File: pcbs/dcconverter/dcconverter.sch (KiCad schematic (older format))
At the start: 49 parts, among them IC1 NCP7805TG, J1 190-9991, J2 Conn_01x01, J3 Conn_01x01, J4 146-8335, J5 Conn_01x01, J6 Conn_01x01, J7 766-6604, J8 766-6604, Q1 NGTB40N120FL2WG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

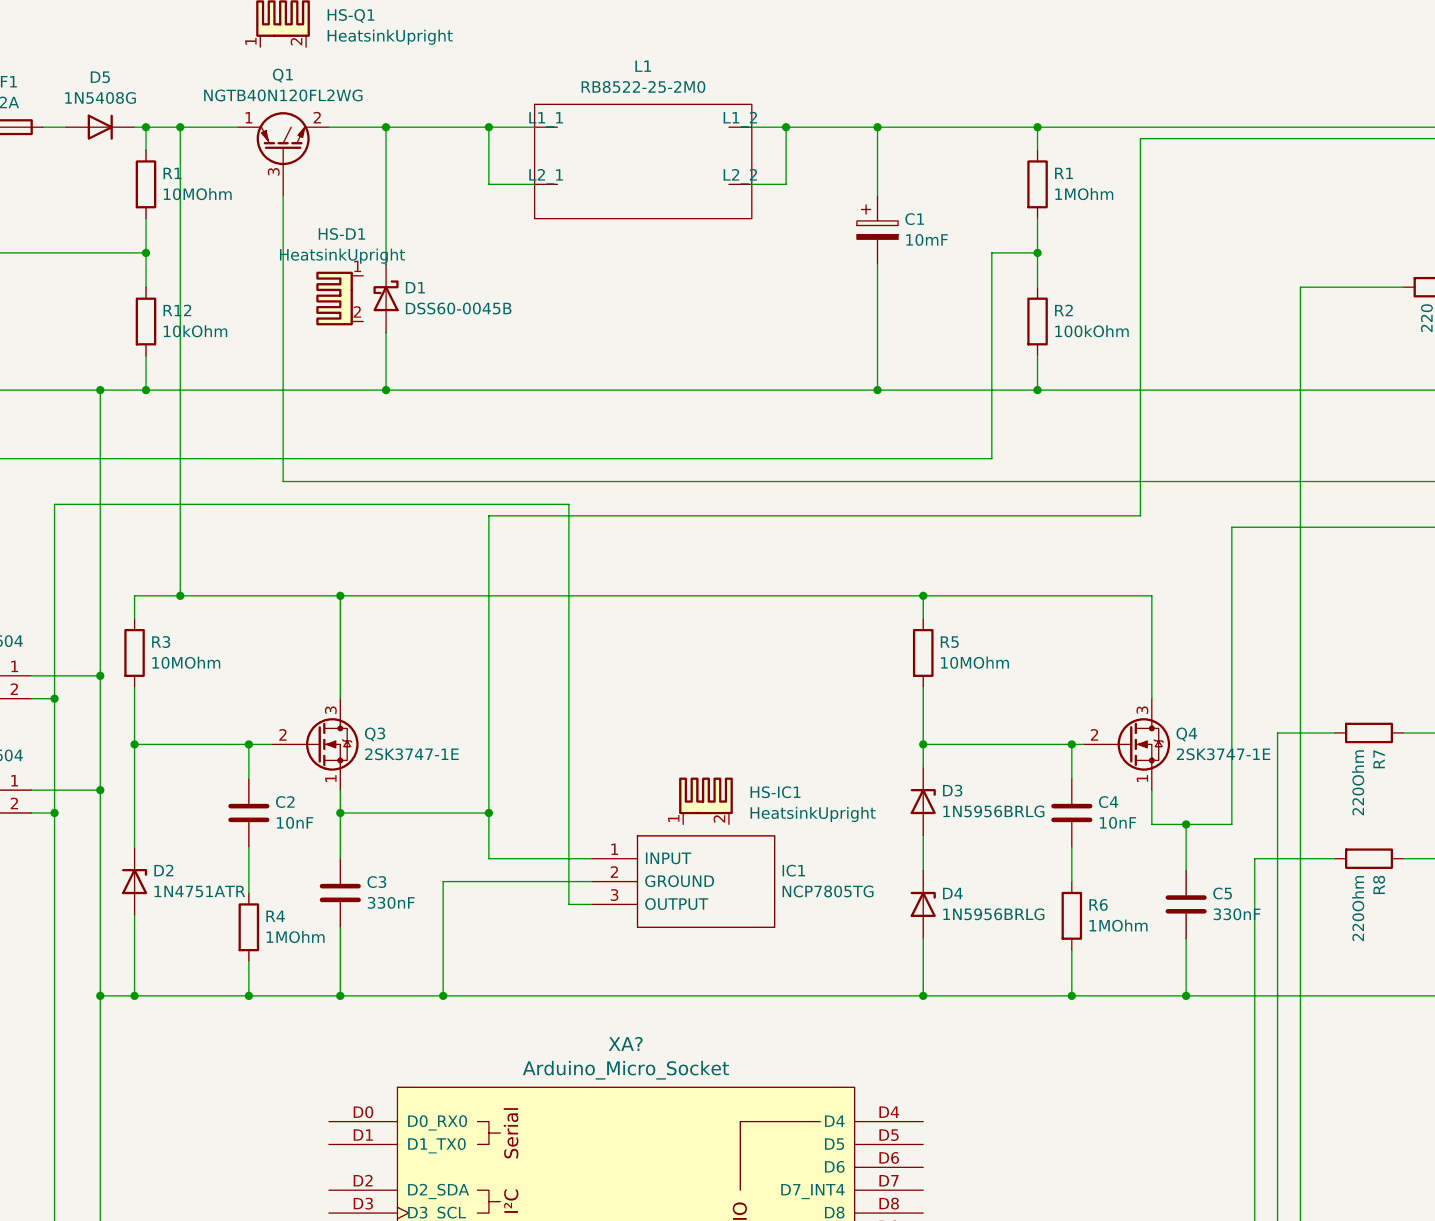
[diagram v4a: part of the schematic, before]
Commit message: Add missing footprints
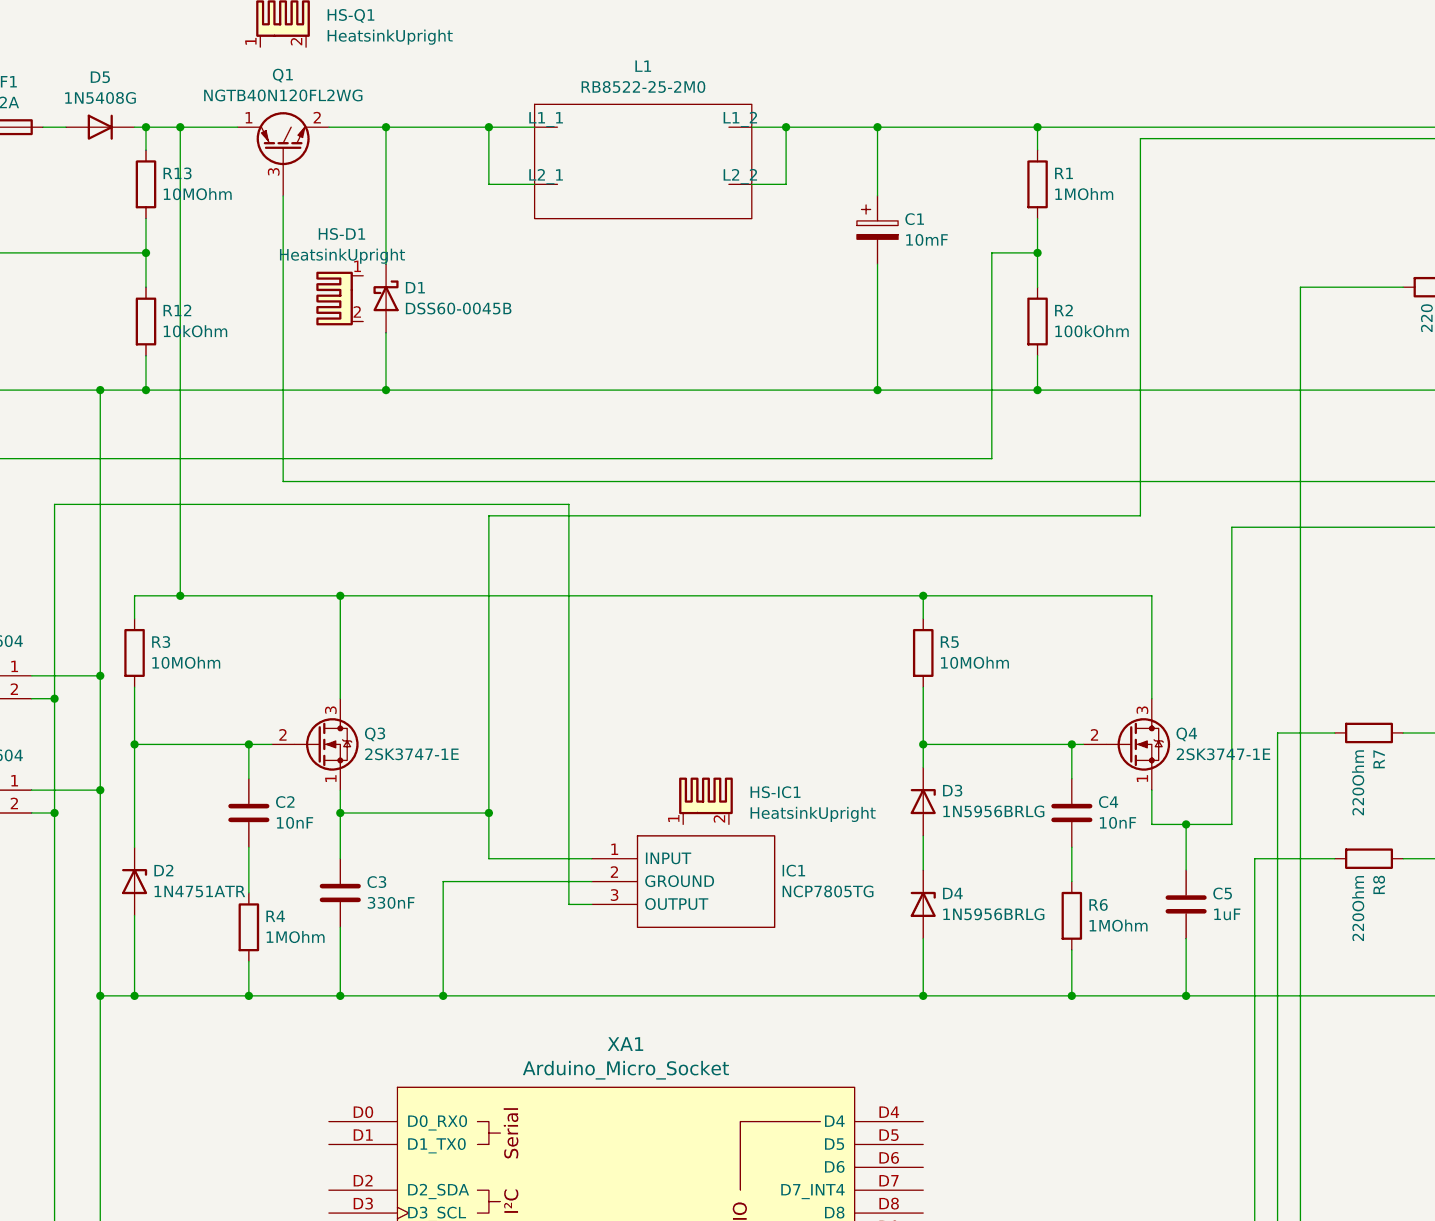
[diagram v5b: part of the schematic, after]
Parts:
- C2, C4: footprint (none) -> Capacitor_THT:C_Disc_D14.5mm_W5.0mm_P7.50mm
- C5: value 330nF -> 1uF; footprint (none) -> Capacitor_THT:CP_Radial_D5.0mm_P2.00mm
- gave numbers to parts that had none: 1
- renumbered R1 to R13
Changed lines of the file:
@@
 F 0 "C2" H 2415 4246 50  0000 L CNN
 F 1 "10nF" H 2415 4155 50  0000 L CNN
-F 2 "" H 2338 4050 50  0001 C CNN
+F 2 "Capacitor_THT:C_Disc_D14.5mm_W5.0mm_P7.50mm" H 2338 4050 50  0001 C CNN
 F 3 "~" H 2300 4200 50  0001 C CNN
 	1    2300 4200
@@
 F 0 "C4" H 6015 4246 50  0000 L CNN
 F 1 "10nF" H 6015 4155 50  0000 L CNN
-F 2 "" H 5938 4050 50  0001 C CNN
+F 2 "Capacitor_THT:C_Disc_D14.5mm_W5.0mm_P7.50mm" H 5938 4050 50  0001 C CNN
 F 3 "~" H 5900 4200 50  0001 C CNN
 	1    5900 4200
@@
 P 6400 4600
 F 0 "C5" H 6515 4646 50  0000 L CNN
-F 1 "330nF" H 6515 4555 50  0000 L CNN
-F 2 "" H 6438 4450 50  0001 C CNN
+F 1 "1uF" H 6515 4555 50  0000 L CNN
+F 2 "Capacitor_THT:CP_Radial_D5.0mm_P2.00mm" H 6438 4450 50  0001 C CNN
 F 3 "~" H 6400 4600 50  0001 C CNN
 	1    6400 4600
@@
 	1650 2350 1850 2350
 $Comp
-L Device:R R1
+L Device:R R13
 U 1 1 5FBBC80C
 P 1850 1450
-F 0 "R1" H 1920 1496 50  0000 L CNN
+F 0 "R13" H 1920 1496 50  0000 L CNN
 F 1 "10MOhm" H 1920 1405 50  0000 L CNN
 F 2 "Resistor_THT:R_Axial_DIN0207_L6.3mm_D2.5mm_P10.16mm_Horizontal" V 1780 1450 50  0001 C CNN
@@
 	1850 2350 2900 2350
 $Comp
-L Custom:Arduino_Micro_Socket XA?
+L Custom:Arduino_Micro_Socket XA1
 U 1 1 5FBF5E9B
 P 3950 6450
-F 0 "XA?" H 3950 7687 60  0000 C CNN
+F 0 "XA1" H 3950 7687 60  0000 C CNN
 F 1 "Arduino_Micro_Socket" H 3950 7581 60  0000 C CNN
 F 2 "Custom:Arduino_Micro_Socket" H 5750 10200 60  0001 C CNN

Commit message: Empty PCB
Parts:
- C3: value 330nF -> 1uF; footprint (none) -> Capacitor_THT:CP_Radial_D5.0mm_P2.00mm
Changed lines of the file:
@@
 P 2700 4550
 F 0 "C3" H 2815 4596 50  0000 L CNN
-F 1 "330nF" H 2815 4505 50  0000 L CNN
-F 2 "" H 2738 4400 50  0001 C CNN
+F 1 "1uF" H 2815 4505 50  0000 L CNN
+F 2 "Capacitor_THT:CP_Radial_D5.0mm_P2.00mm" H 2738 4400 50  0001 C CNN
 F 3 "~" H 2700 4550 50  0001 C CNN
 	1    2700 4550

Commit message: Fix Heatsinks
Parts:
- C3, C5: footprint Capacitor_THT:CP_Radial_D5.0mm_P2.00mm -> Capacitor_THT:CP_Radial_D8.0mm_P2.50mm
- HS-D1, HS-IC1, HS-Q1, HS-Q2: symbol Mechanical:Heatsink_Pad_2Pin -> Mechanical:Heatsink
- J7, J8: value 766-6604 -> 483-8461; footprint Custom:CES-102-XX-Y-S -> Custom:Molex_KK_254_2pin
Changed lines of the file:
@@
 $EndComp
 $Comp
-L Mechanical:Heatsink_Pad_2Pin HS-Q1
+L Mechanical:Heatsink HS-Q1
 U 1 1 5F93ACCE
 P 2450 750
@@
 	2900 1200 2650 1200
 $Comp
-L Mechanical:Heatsink_Pad_2Pin HS-D1
+L Mechanical:Heatsink HS-D1
 U 1 1 5F93F452
 P 2700 1950
@@
 	5750 1750 5750 1900
 $Comp
-L Mechanical:Heatsink_Pad_2Pin HS-Q2
+L Mechanical:Heatsink HS-Q2
 U 1 1 5F94C442
 P 8600 750
@@
 	3350 4400 3350 4200
 $Comp
-L Mechanical:Heatsink_Pad_2Pin HS-IC1
+L Mechanical:Heatsink HS-IC1
 U 1 1 5F955A4D
 P 4300 4150
@@
 P 1150 3600
 F 0 "J7" H 1150 3850 50  0000 C CNN
-F 1 "766-6604" H 1150 3750 50  0000 C CNN
-F 2 "Custom:CES-102-XX-Y-S" H 1150 3600 50  0001 C CNN
+F 1 "483-8461" H 1150 3750 50  0000 C CNN
+F 2 "Custom:Molex_KK_254_2pin" H 1150 3600 50  0001 C CNN
 F 3 "~" H 1150 3600 50  0001 C CNN
 	1    1150 3600
@@
 P 1150 4100
 F 0 "J8" H 1150 4350 50  0000 C CNN
-F 1 "766-6604" H 1150 4250 50  0000 C CNN
-F 2 "Custom:CES-102-XX-Y-S" H 1150 4100 50  0001 C CNN
+F 1 "483-8461" H 1150 4250 50  0000 C CNN
+F 2 "Custom:Molex_KK_254_2pin" H 1150 4100 50  0001 C CNN
 F 3 "~" H 1150 4100 50  0001 C CNN
 	1    1150 4100
@@
 F 0 "C3" H 2815 4596 50  0000 L CNN
 F 1 "1uF" H 2815 4505 50  0000 L CNN
-F 2 "Capacitor_THT:CP_Radial_D5.0mm_P2.00mm" H 2738 4400 50  0001 C CNN
+F 2 "Capacitor_THT:CP_Radial_D8.0mm_P2.50mm" H 2738 4400 50  0001 C CNN
 F 3 "~" H 2700 4550 50  0001 C CNN
 	1    2700 4550
@@
 F 0 "C5" H 6515 4646 50  0000 L CNN
 F 1 "1uF" H 6515 4555 50  0000 L CNN
-F 2 "Capacitor_THT:CP_Radial_D5.0mm_P2.00mm" H 6438 4450 50  0001 C CNN
+F 2 "Capacitor_THT:CP_Radial_D8.0mm_P2.50mm" H 6438 4450 50  0001 C CNN
 F 3 "~" H 6400 4600 50  0001 C CNN
 	1    6400 4600
